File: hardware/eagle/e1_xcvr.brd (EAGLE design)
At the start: 50 x 50 mm, 48 parts, among them T1 BC847C, U1 IDT82V2081, U3_2M 2.048 Mhz, U4_1M5 1.544 MHz, U6 TPS736XX

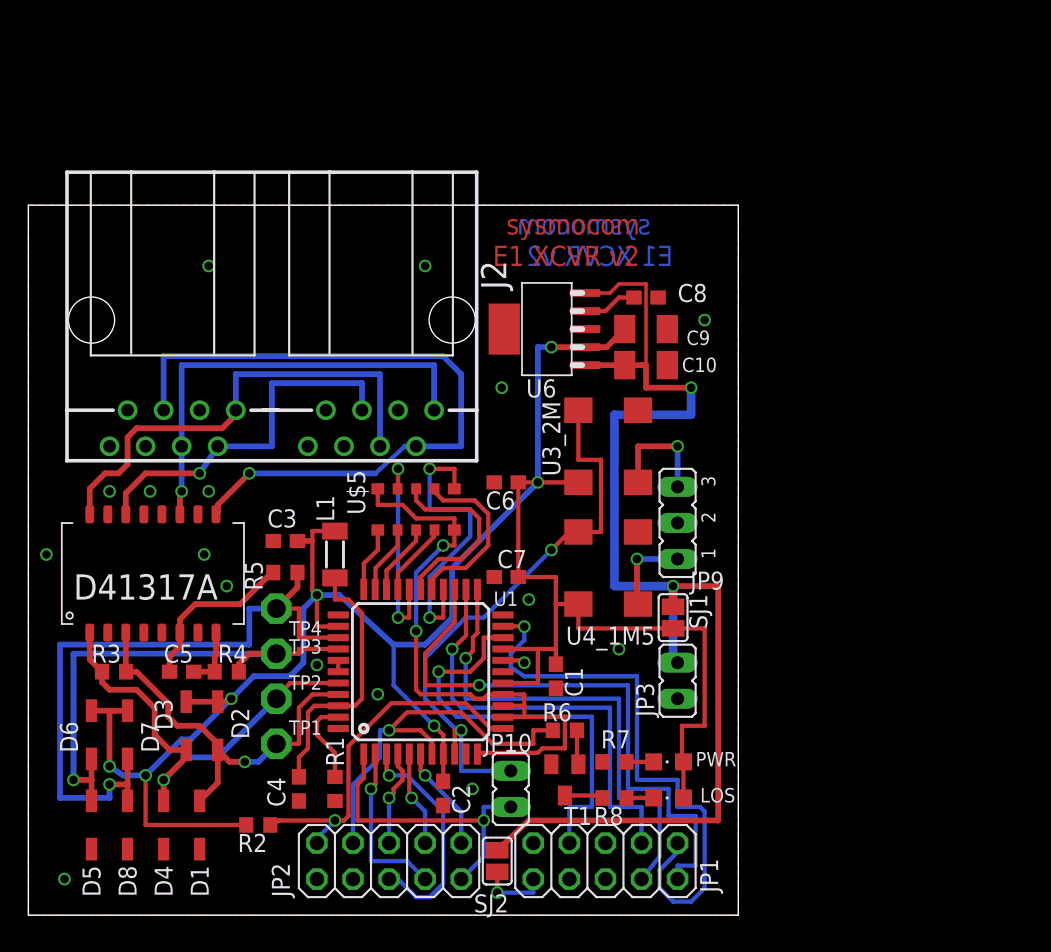
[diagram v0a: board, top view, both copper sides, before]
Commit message: enlarge board to have proper mounting holes for mechanical mounting
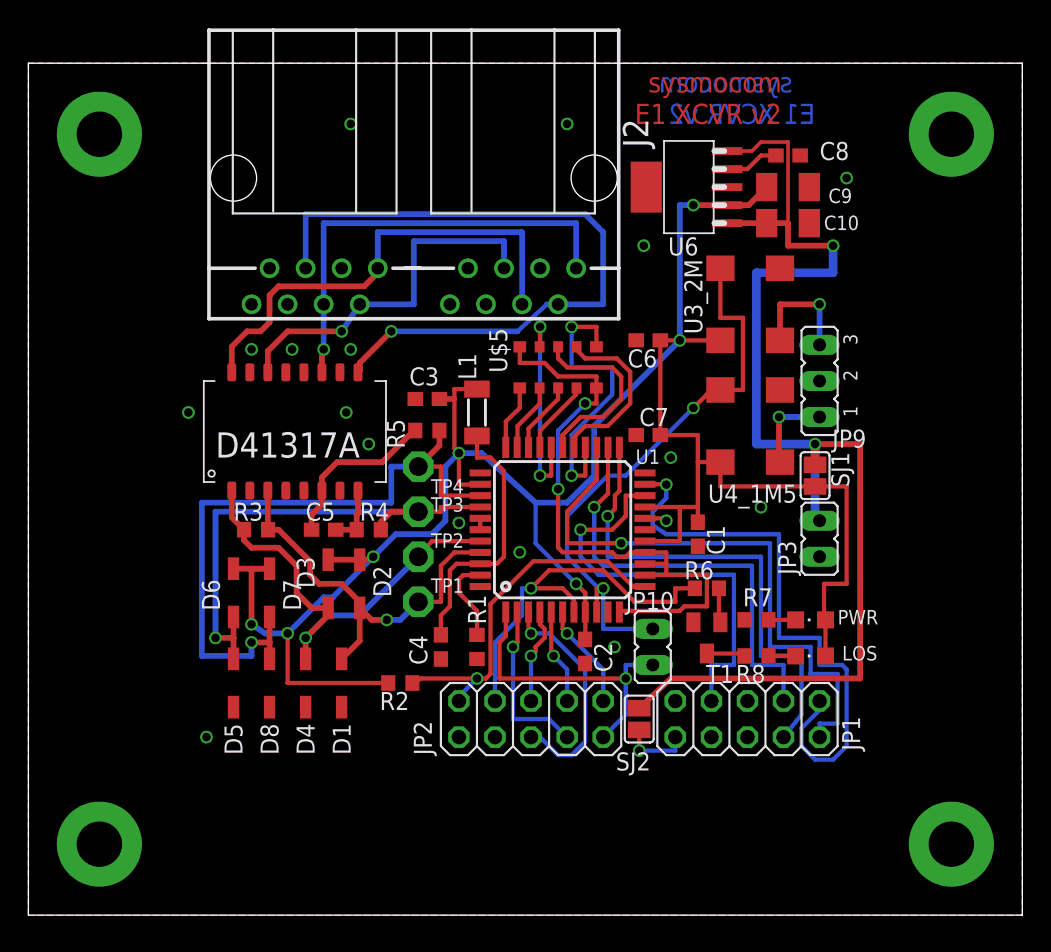
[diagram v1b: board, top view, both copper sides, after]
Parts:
- moved D1 14.1 mm to (22.1, 16.4)
- moved JP9 14.1 mm to (55.7, 37.6)
- moved R5 14.1 mm to (28.1, 34.1)
- moved U$2 14.1 mm to (18.6, 34.1)
- moved U$5 14.1 mm to (37.3, 38.6)
- moved U1 14.1 mm to (37.6, 27.1)
- moved C1 14.1 mm to (47.1, 26.8)
- moved C10 14.1 mm to (53.5, 48.7)
- moved C2 14.1 mm to (39.2, 18.6)
- moved C3 14.1 mm to (28.1, 36.4)
- moved C4 14.1 mm to (29.1, 18.9)
- moved C5 14.1 mm to (20.8, 27.1)
- moved C7 14.1 mm to (43.7, 33.8)
- moved C8 14.1 mm to (53.5, 53.5)
- moved C9 14.1 mm to (53.5, 51.3)
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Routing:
- net GND: vias 19 -> 23
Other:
- board size 50 x 50 mm -> 70 x 60 mm

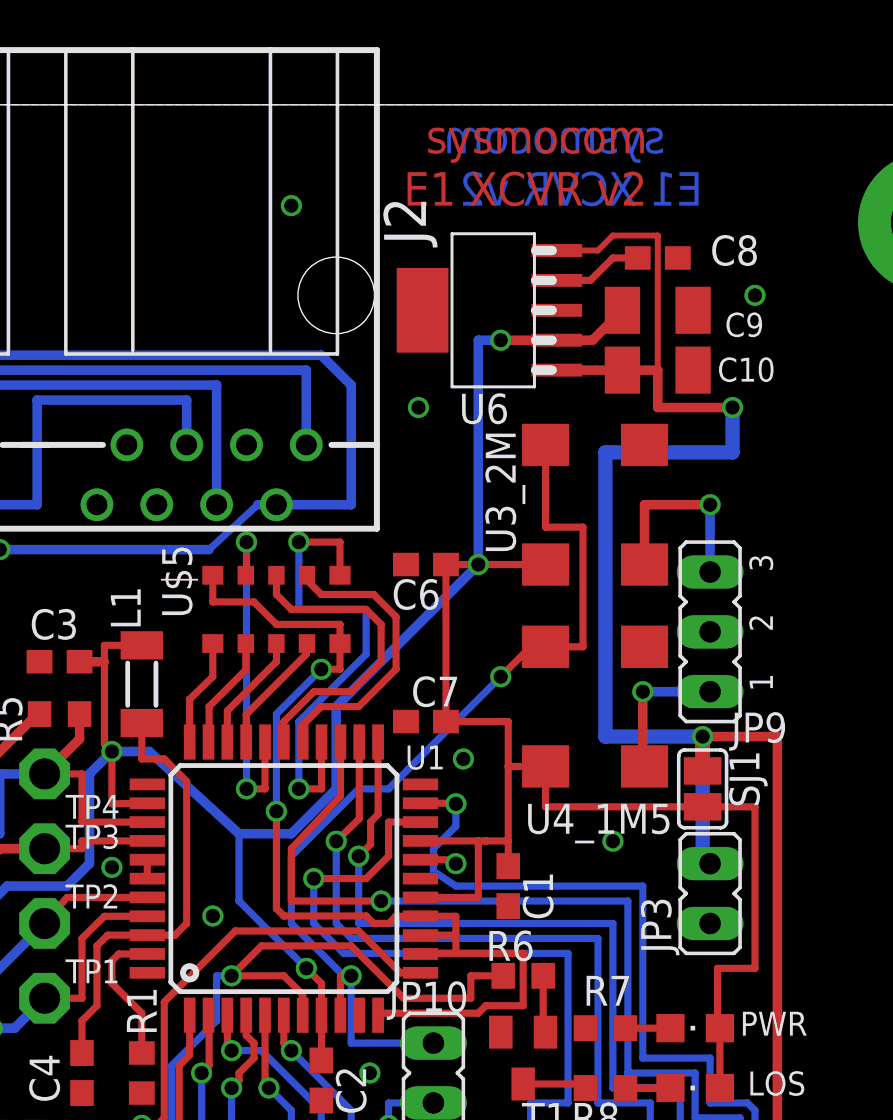
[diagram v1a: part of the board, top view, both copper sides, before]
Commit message: increase clearance of ground planes; pad roundness
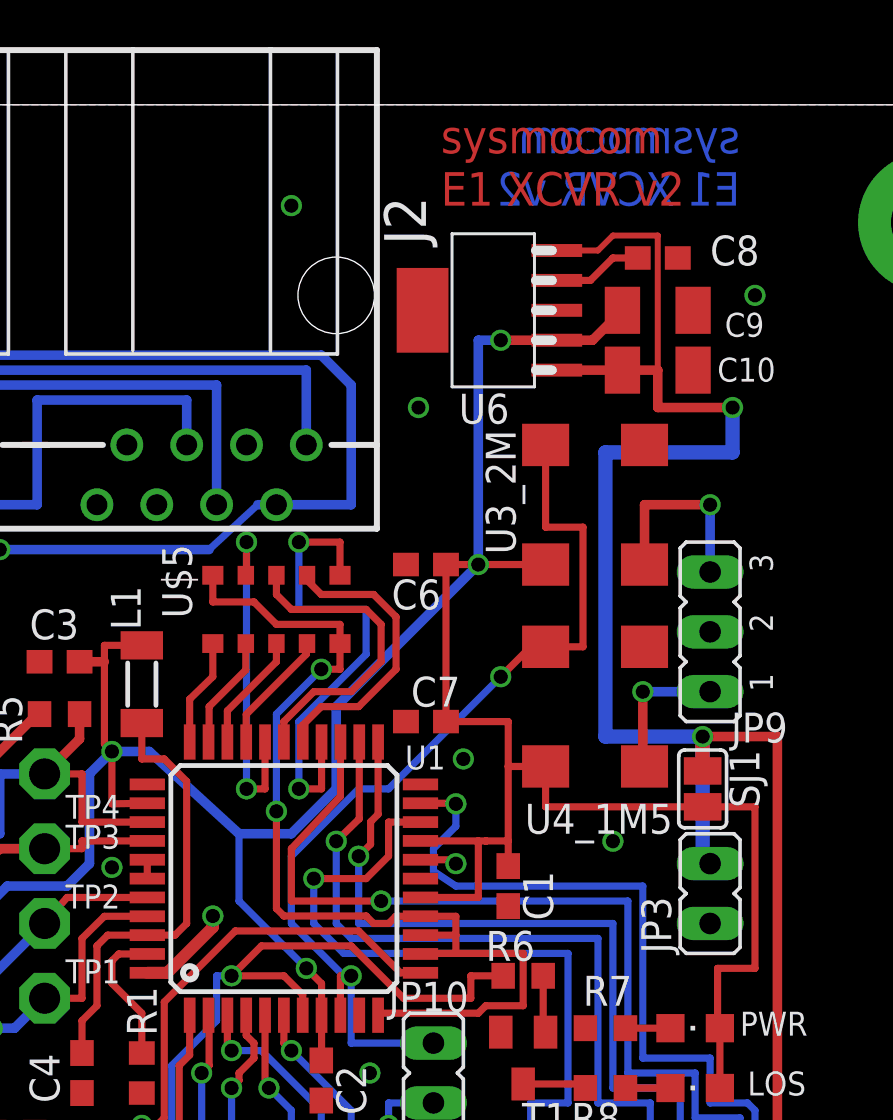
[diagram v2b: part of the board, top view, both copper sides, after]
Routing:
- net GND: track 47.1 -> 51.2 mm
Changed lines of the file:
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@@
 <layer number="2" name="Route2" color="1" fill="3" visible="no" active="no"/>
 <layer number="3" name="Route3" color="4" fill="3" visible="no" active="no"/>
+<layer number="4" name="Route4" color="1" fill="4" visible="no" active="yes"/>
+<layer number="5" name="Route5" color="4" fill="4" visible="no" active="yes"/>
+<layer number="6" name="Route6" color="1" fill="8" visible="no" active="yes"/>
+<layer number="7" name="Route7" color="4" fill="8" visible="no" active="yes"/>
+<layer number="8" name="Route8" color="1" fill="2" visible="no" active="yes"/>
+<layer number="9" name="Route9" color="4" fill="2" visible="no" active="yes"/>
+<layer number="10" name="Route10" color="1" fill="7" visible="no" active="yes"/>
+<layer number="11" name="Route11" color="4" fill="7" visible="no" active="yes"/>
+<layer number="12" name="Route12" color="1" fill="5" visible="no" active="yes"/>
+<layer number="13" name="Route13" color="4" fill="5" visible="no" active="yes"/>
 <layer number="14" name="Route14" color="1" fill="6" visible="no" active="no"/>
 <layer number="15" name="Route15" color="4" fill="6" visible="no" active="no"/>
@@
 <wire x1="70" y1="60" x2="0" y2="60" width="0" layer="20"/>
 <wire x1="0" y1="60" x2="0" y2="0" width="0" layer="20"/>
-<text x="53.815" y="57.9425" size="1.4224" layer="16" font="vector" ratio="14" rot="MR0">sysmocom</text>
-<text x="55.4025" y="55.72" size="1.4224" layer="16" font="vector" ratio="14" rot="MR0">E1 XCVR v2</text>
-<text x="43.655" y="57.9425" size="1.4224" layer="1" font="vector" ratio="14">sysmocom</text>
-<text x="42.7025" y="55.72" size="1.4224" layer="1" font="vector" ratio="14">E1 XCVR v2</text>
+<text x="56.99" y="57.9425" size="1.4224" layer="16" font="vector" ratio="14" rot="MR0">sysmocom</text>
+<text x="56.99" y="55.72" size="1.4224" layer="16" font="vector" ratio="14" rot="MR0">E1 XCVR v2</text>
+<text x="44.29" y="57.9425" size="1.4224" layer="1" font="vector" ratio="14">sysmocom</text>
+<text x="44.29" y="55.72" size="1.4224" layer="1" font="vector" ratio="14">E1 XCVR v2</text>
 <text x="13.175" y="32.225" size="1.778" layer="25">D41317A</text>
 </plain>
@@
 </class>
 </classes>
-<designrules name="default">
+<designrules name="default *">
 <description language="de">&lt;b&gt;EAGLE Design Rules&lt;/b&gt;
 &lt;p&gt;
@@
 <param name="mtCopper" value="0.035mm 0.035mm 0.035mm 0.035mm 0.035mm 0.035mm 0.035mm 0.035mm 0.035mm 0.035mm 0.035mm 0.035mm 0.035mm 0.035mm 0.035mm 0.035mm"/>
 <param name="mtIsolate" value="1.5mm 0.15mm 0.2mm 0.15mm 0.2mm 0.15mm 0.2mm 0.15mm 0.2mm 0.15mm 0.2mm 0.15mm 0.2mm 0.15mm 0.2mm"/>
-<param name="mdWireWire" value="6mil"/>
-<param name="mdWirePad" value="6mil"/>
-<param name="mdWireVia" value="6mil"/>
+<param name="mdWireWire" value="8mil"/>
+<param name="mdWirePad" value="8mil"/>
+<param name="mdWireVia" value="8mil"/>
 <param name="mdPadPad" value="6mil"/>
 <param name="mdPadVia" value="6mil"/>
@@
 <param name="mlMaxCreamFrame" value="0mil"/>
 <param name="mlViaStopLimit" value="100mil"/>
-<param name="srRoundness" value="0"/>
+<param name="srRoundness" value="0.3"/>
 <param name="srMinRoundness" value="0mil"/>
-<param name="srMaxRoundness" value="0mil"/>
+<param name="srMaxRoundness" value="10mil"/>
 <param name="slThermalIsolate" value="10mil"/>
 <param name="slThermalsForVias" value="0"/>
@@
 <contactref element="C6" pad="2"/>
 <contactref element="C7" pad="1"/>
-<contactref element="U4_1M5" pad="P$2"/>
 <contactref element="JP9" pad="2"/>
 <contactref element="D5" pad="2"/>
@@
 <via x="65" y="5" extent="1-16" drill="3.2" diameter="6"/>
 <via x="65" y="55" extent="1-16" drill="3.2" diameter="6"/>
+<wire x1="31.8225" y1="23.145" x2="32.67" y2="23.145" width="0.508" layer="1"/>
+<wire x1="32.67" y1="23.145" x2="34.60625" y2="25.08125" width="0.508" layer="1"/>
+<wire x1="34.60625" y1="25.08125" x2="34.60625" y2="25.5575" width="0.508" layer="1"/>
 </signal>
 <signal name="N$1">
